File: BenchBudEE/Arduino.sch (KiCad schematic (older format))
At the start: 19 parts

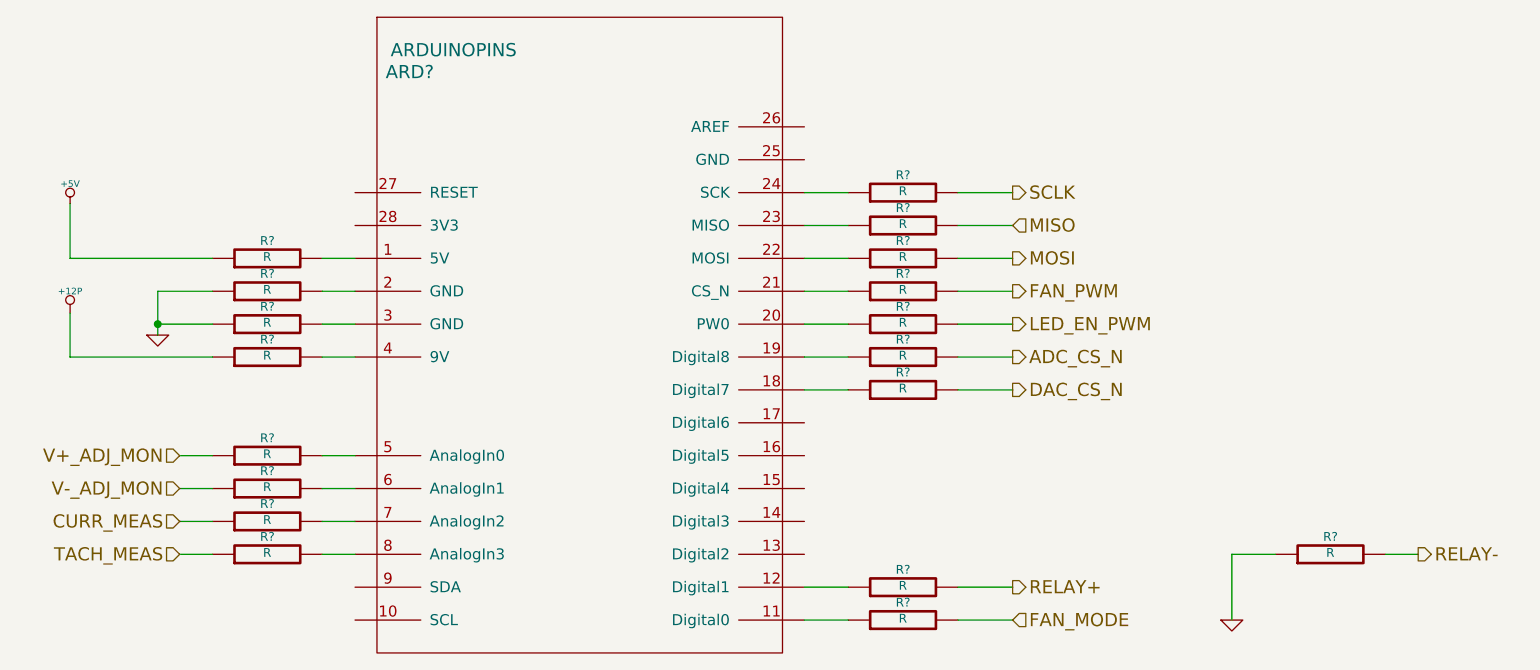
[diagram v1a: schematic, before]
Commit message: Associating and Placing the Relay Module
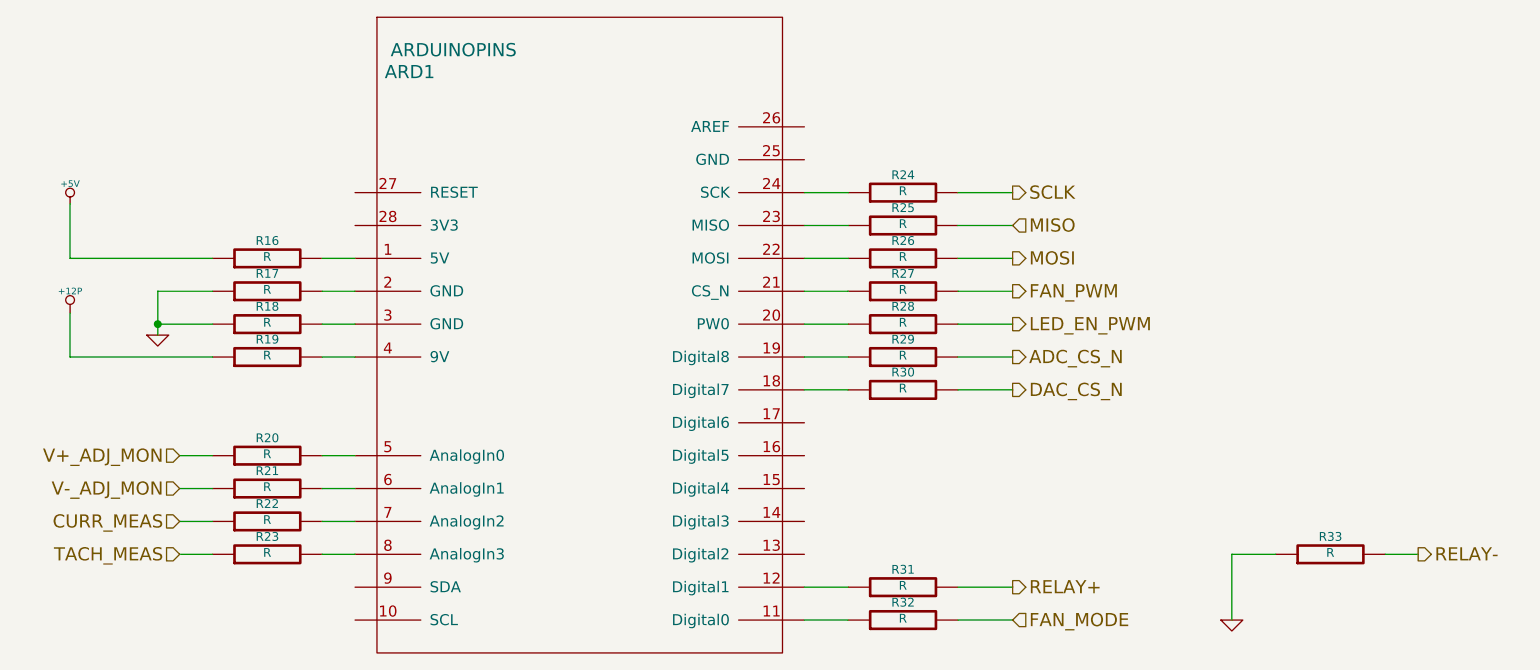
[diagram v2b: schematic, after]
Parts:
- gave numbers to parts that had none: 19
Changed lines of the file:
@@
 CURR_MEAS
 $Comp
-L R R?
+L R R27
 U 1 1 52F7E8CB
 P 6200 4350
-F 0 "R?" V 6280 4350 40  0000 C CNN
+F 0 "R27" V 6280 4350 40  0000 C CNN
 F 1 "R" V 6207 4351 40  0000 C CNN
 F 2 "~" V 6130 4350 30  0000 C CNN
@@
 	6450 4350 6700 4350
 $Comp
-L R R?
+L R R31
 U 1 1 52F7FF15
 P 6200 5700
-F 0 "R?" V 6280 5700 40  0000 C CNN
+F 0 "R31" V 6280 5700 40  0000 C CNN
 F 1 "R" V 6207 5701 40  0000 C CNN
 F 2 "~" V 6130 5700 30  0000 C CNN
@@
 	7700 5550 7700 5850
 $Comp
-L GND #PWR034
+L GND #PWR39
 U 1 1 52F7FF5C
 P 7700 5850
-F 0 "#PWR034" H 7700 5850 30  0001 C CNN
+F 0 "#PWR39" H 7700 5850 30  0001 C CNN
 F 1 "GND" H 7700 5780 30  0001 C CNN
 F 2 "" H 7700 5850 60  0000 C CNN
@@
 $EndComp
 $Comp
-L R R?
+L R R22
 U 1 1 52F7FF69
 P 3300 5400
-F 0 "R?" V 3380 5400 40  0000 C CNN
+F 0 "R22" V 3380 5400 40  0000 C CNN
 F 1 "R" V 3307 5401 40  0000 C CNN
 F 2 "~" V 3230 5400 30  0000 C CNN
@@
 $EndComp
 $Comp
-L R R?
+L R R23
 U 1 1 52F7FF6F
 P 3300 5550
-F 0 "R?" V 3380 5550 40  0000 C CNN
+F 0 "R23" V 3380 5550 40  0000 C CNN
 F 1 "R" V 3307 5551 40  0000 C CNN
 F 2 "~" V 3230 5550 30  0000 C CNN
@@
 V-_ADJ_MON
 $Comp
-L R R?
+L R R21
 U 1 1 52F82BA9
 P 3300 5250
-F 0 "R?" V 3380 5250 40  0000 C CNN
+F 0 "R21" V 3380 5250 40  0000 C CNN
 F 1 "R" V 3307 5251 40  0000 C CNN
 F 2 "~" V 3230 5250 30  0000 C CNN
@@
 $EndComp
 $Comp
-L R R?
+L R R20
 U 1 1 52F82BAF
 P 3300 5100
-F 0 "R?" V 3380 5100 40  0000 C CNN
+F 0 "R20" V 3380 5100 40  0000 C CNN
 F 1 "R" V 3307 5101 40  0000 C CNN
 F 2 "~" V 3230 5100 30  0000 C CNN
@@
 	3550 5100 3700 5100
 $Comp
-L R R?
+L R R30
 U 1 1 52F82BF7
 P 6200 4800
-F 0 "R?" V 6280 4800 40  0000 C CNN
+F 0 "R30" V 6280 4800 40  0000 C CNN
 F 1 "R" V 6207 4801 40  0000 C CNN
 F 2 "~" V 6130 4800 30  0000 C CNN
@@
 $EndComp
 $Comp
-L R R?
+L R R26
 U 1 1 52F82BFD
 P 6200 4200
-F 0 "R?" V 6280 4200 40  0000 C CNN
+F 0 "R26" V 6280 4200 40  0000 C CNN
 F 1 "R" V 6207 4201 40  0000 C CNN
 F 2 "~" V 6130 4200 30  0000 C CNN
@@
 $EndComp
 $Comp
-L R R?
+L R R25
 U 1 1 52F82C03
 P 6200 4050
-F 0 "R?" V 6280 4050 40  0000 C CNN
+F 0 "R25" V 6280 4050 40  0000 C CNN
 F 1 "R" V 6207 4051 40  0000 C CNN
 F 2 "~" V 6130 4050 30  0000 C CNN
@@
 $EndComp
 $Comp
-L R R?
+L R R24
 U 1 1 52F82C09
 P 6200 3900
-F 0 "R?" V 6280 3900 40  0000 C CNN
+F 0 "R24" V 6280 3900 40  0000 C CNN
 F 1 "R" V 6207 3901 40  0000 C CNN
 F 2 "~" V 6130 3900 30  0000 C CNN
@@
 	6700 3900 6450 3900
 $Comp
-L R R?
+L R R33
 U 1 1 52F82CA5
 P 8150 5550
-F 0 "R?" V 8230 5550 40  0000 C CNN
+F 0 "R33" V 8230 5550 40  0000 C CNN
 F 1 "R" V 8157 5551 40  0000 C CNN
 F 2 "~" V 8080 5550 30  0000 C CNN
@@
 LED_EN_PWM
 $Comp
-L R R?
+L R R28
 U 1 1 52F82CFD
 P 6200 4500
-F 0 "R?" V 6280 4500 40  0000 C CNN
+F 0 "R28" V 6280 4500 40  0000 C CNN
 F 1 "R" V 6207 4501 40  0000 C CNN
 F 2 "~" V 6130 4500 30  0000 C CNN
@@
 	6450 4500 6700 4500
 $Comp
-L R R?
+L R R29
 U 1 1 52F85651
 P 6200 4650
-F 0 "R?" V 6280 4650 40  0000 C CNN
+F 0 "R29" V 6280 4650 40  0000 C CNN
 F 1 "R" V 6207 4651 40  0000 C CNN
 F 2 "~" V 6130 4650 30  0000 C CNN
@@
 FAN_MODE
 $Comp
-L R R?
+L R R32
 U 1 1 52FACCB6
 P 6200 5850
-F 0 "R?" V 6280 5850 40  0000 C CNN
+F 0 "R32" V 6280 5850 40  0000 C CNN
 F 1 "R" V 6207 5851 40  0000 C CNN
 F 2 "~" V 6130 5850 30  0000 C CNN
@@
 	6450 5850 6700 5850
 $Comp
-L R R?
+L R R19
 U 1 1 52FACD1D
 P 3300 4650
-F 0 "R?" V 3380 4650 40  0000 C CNN
+F 0 "R19" V 3380 4650 40  0000 C CNN
 F 1 "R" V 3307 4651 40  0000 C CNN
 F 2 "~" V 3230 4650 30  0000 C CNN
@@
 	2400 4650 2400 4450
 $Comp
-L +12P #PWR035
+L +12P #PWR37
 U 1 1 52FACD63
 P 2400 4450
-F 0 "#PWR035" H 2400 4420 30  0001 C CNN
+F 0 "#PWR37" H 2400 4420 30  0001 C CNN
 F 1 "+12P" H 2400 4550 30  0000 C CNN
 F 2 "" H 2400 4450 60  0000 C CNN
@@
 $EndComp
 $Comp
-L ARDUINOPINS ARD?
+L ARDUINOPINS ARD1
 U 1 1 52FF78C8
 P 4750 4650
-F 0 "ARD?" H 3950 5950 60  0000 C CNN
+F 0 "ARD1" H 3950 5950 60  0000 C CNN
 F 1 "ARDUINOPINS" H 4150 6050 60  0000 C CNN
 F 2 "~" H 4450 3700 60  0000 C CNN
@@
 	2400 4200 2400 3950
 $Comp
-L +5V #PWR036
+L +5V #PWR36
 U 1 1 5300B8CD
 P 2400 3950
-F 0 "#PWR036" H 2400 4040 20  0001 C CNN
+F 0 "#PWR36" H 2400 4040 20  0001 C CNN
 F 1 "+5V" H 2400 4040 30  0000 C CNN
 F 2 "" H 2400 3950 60  0000 C CNN
@@
 $EndComp
 $Comp
-L R R?
+L R R16
 U 1 1 5300B8E0
 P 3300 4200
-F 0 "R?" V 3380 4200 40  0000 C CNN
+F 0 "R16" V 3380 4200 40  0000 C CNN
 F 1 "R" V 3307 4201 40  0000 C CNN
 F 2 "~" V 3230 4200 30  0000 C CNN
@@
 $EndComp
 $Comp
-L R R?
+L R R17
 U 1 1 5300B8E6
 P 3300 4350
-F 0 "R?" V 3380 4350 40  0000 C CNN
+F 0 "R17" V 3380 4350 40  0000 C CNN
 F 1 "R" V 3307 4351 40  0000 C CNN
 F 2 "~" V 3230 4350 30  0000 C CNN
@@
 $EndComp
 $Comp
-L R R?
+L R R18
 U 1 1 5300B8EC
 P 3300 4500
-F 0 "R?" V 3380 4500 40  0000 C CNN
+F 0 "R18" V 3380 4500 40  0000 C CNN
 F 1 "R" V 3307 4501 40  0000 C CNN
 F 2 "~" V 3230 4500 30  0000 C CNN
@@
 Connection ~ 2800 4500
 $Comp
-L GND #PWR037
+L GND #PWR38
 U 1 1 5300B9FD
 P 2800 4550
-F 0 "#PWR037" H 2800 4550 30  0001 C CNN
+F 0 "#PWR38" H 2800 4550 30  0001 C CNN
 F 1 "GND" H 2800 4480 30  0001 C CNN
 F 2 "" H 2800 4550 60  0000 C CNN

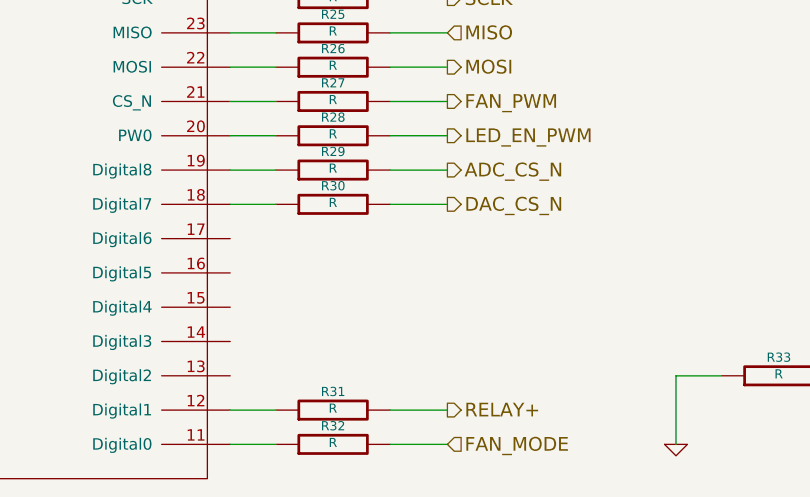
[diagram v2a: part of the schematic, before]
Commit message: Associating and Placingthe Thermocouple Module
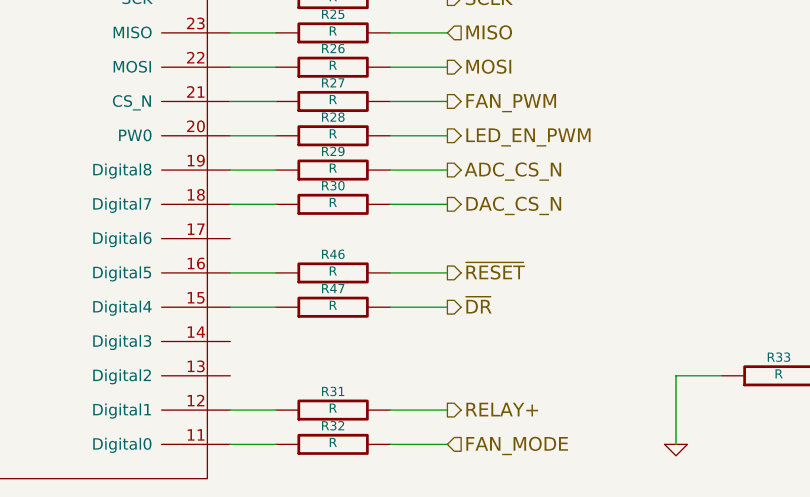
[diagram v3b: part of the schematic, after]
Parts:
- added R46, R47: R, ~, symbol R
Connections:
- net at ARD1.15 (Digital4): now also R47.1
- net at ARD1.16 (Digital5): now also R46.1
- new net ~DR: R47.2
- new net ~RESET: R46.2
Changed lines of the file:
@@
 Sheet 7 9
 Title ""
-Date "17 feb 2014"
+Date "19 feb 2014"
 Rev ""
 Comp ""
@@
 	7700 5550 7700 5850
 $Comp
-L GND #PWR39
+L GND #PWR042
 U 1 1 52F7FF5C
 P 7700 5850
-F 0 "#PWR39" H 7700 5850 30  0001 C CNN
+F 0 "#PWR042" H 7700 5850 30  0001 C CNN
 F 1 "GND" H 7700 5780 30  0001 C CNN
 F 2 "" H 7700 5850 60  0000 C CNN
@@
 	2400 4650 2400 4450
 $Comp
-L +12P #PWR37
+L +12P #PWR043
 U 1 1 52FACD63
 P 2400 4450
-F 0 "#PWR37" H 2400 4420 30  0001 C CNN
+F 0 "#PWR043" H 2400 4420 30  0001 C CNN
 F 1 "+12P" H 2400 4550 30  0000 C CNN
 F 2 "" H 2400 4450 60  0000 C CNN
@@
 	2400 4200 2400 3950
 $Comp
-L +5V #PWR36
+L +5V #PWR044
 U 1 1 5300B8CD
 P 2400 3950
-F 0 "#PWR36" H 2400 4040 20  0001 C CNN
+F 0 "#PWR044" H 2400 4040 20  0001 C CNN
 F 1 "+5V" H 2400 4040 30  0000 C CNN
 F 2 "" H 2400 3950 60  0000 C CNN
@@
 Connection ~ 2800 4500
 $Comp
-L GND #PWR38
+L GND #PWR045
 U 1 1 5300B9FD
 P 2800 4550
-F 0 "#PWR38" H 2800 4550 30  0001 C CNN
+F 0 "#PWR045" H 2800 4550 30  0001 C CNN
 F 1 "GND" H 2800 4480 30  0001 C CNN
 F 2 "" H 2800 4550 60  0000 C CNN
@@
 	1    0    0    -1
 $EndComp
+Text HLabel 6700 5250 2    60   Output ~ 0
+~DR
+$Comp
+L R R47
+U 1 1 53041CC0
+P 6200 5250
+F 0 "R47" V 6280 5250 40  0000 C CNN
+F 1 "R" V 6207 5251 40  0000 C CNN
+F 2 "~" V 6130 5250 30  0000 C CNN
+F 3 "~" H 6200 5250 30  0000 C CNN
+	1    6200 5250
+	0    -1   -1   0
+$EndComp
+Wire Wire Line
+	5750 5250 5950 5250
+Wire Wire Line
+	6450 5250 6700 5250
+$Comp
+L R R46
+U 1 1 53041CC8
+P 6200 5100
+F 0 "R46" V 6280 5100 40  0000 C CNN
+F 1 "R" V 6207 5101 40  0000 C CNN
+F 2 "~" V 6130 5100 30  0000 C CNN
+F 3 "~" H 6200 5100 30  0000 C CNN
+	1    6200 5100
+	0    -1   -1   0
+$EndComp
+Wire Wire Line
+	5750 5100 5950 5100
+Wire Wire Line
+	6450 5100 6700 5100
+Text HLabel 6700 5100 2    60   Output ~ 0
+~RESET
 $EndSCHEMATC

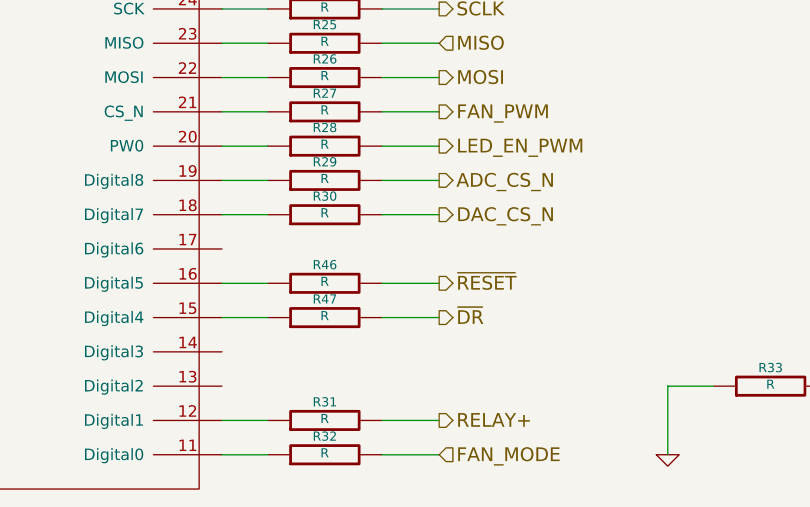
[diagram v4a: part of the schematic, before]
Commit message: Associating and Placing Fan Module
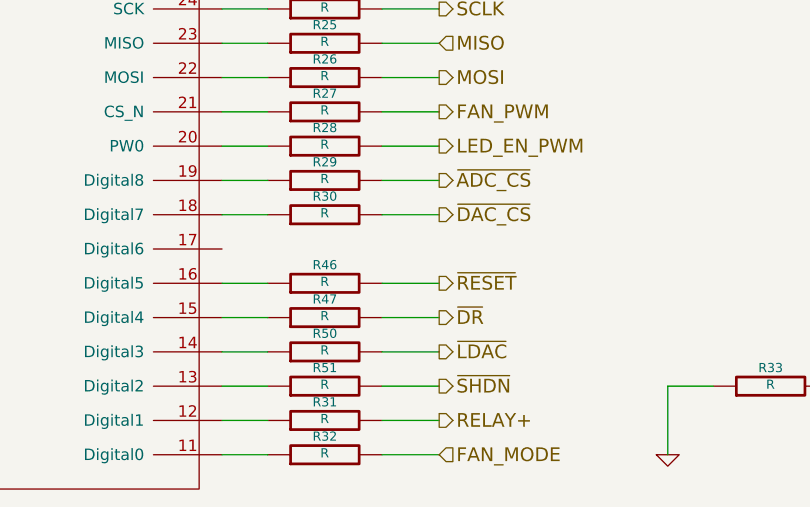
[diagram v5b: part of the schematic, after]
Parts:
- added R50, R51: R, ~, symbol R
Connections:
- net at ARD1.13 (Digital2): now also R51.1
- net at ARD1.14 (Digital3): now also R50.1
- net ADC_CS_N renamed ~ADC_CS
- net DAC_CS_N renamed ~DAC_CS
- new net ~LDAC: R50.2
- new net ~SHDN: R51.2
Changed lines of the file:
@@
 SCLK
 Text HLabel 6700 4800 2    60   Output ~ 0
-DAC_CS_N
+~DAC_CS
 Text HLabel 6700 4350 2    60   Output ~ 0
 FAN_PWM
@@
 	7700 5550 7700 5850
 $Comp
-L GND #PWR042
+L GND #PWR47
 U 1 1 52F7FF5C
 P 7700 5850
-F 0 "#PWR042" H 7700 5850 30  0001 C CNN
+F 0 "#PWR47" H 7700 5850 30  0001 C CNN
 F 1 "GND" H 7700 5780 30  0001 C CNN
 F 2 "" H 7700 5850 60  0000 C CNN
@@
 $EndComp
 Text HLabel 6700 4650 2    60   Output ~ 0
-ADC_CS_N
+~ADC_CS
 Wire Wire Line
 	5750 4650 5950 4650
@@
 	2400 4650 2400 4450
 $Comp
-L +12P #PWR043
+L +12P #PWR45
 U 1 1 52FACD63
 P 2400 4450
-F 0 "#PWR043" H 2400 4420 30  0001 C CNN
+F 0 "#PWR45" H 2400 4420 30  0001 C CNN
 F 1 "+12P" H 2400 4550 30  0000 C CNN
 F 2 "" H 2400 4450 60  0000 C CNN
@@
 	2400 4200 2400 3950
 $Comp
-L +5V #PWR044
+L +5V #PWR44
 U 1 1 5300B8CD
 P 2400 3950
-F 0 "#PWR044" H 2400 4040 20  0001 C CNN
+F 0 "#PWR44" H 2400 4040 20  0001 C CNN
 F 1 "+5V" H 2400 4040 30  0000 C CNN
 F 2 "" H 2400 3950 60  0000 C CNN
@@
 Connection ~ 2800 4500
 $Comp
-L GND #PWR045
+L GND #PWR46
 U 1 1 5300B9FD
 P 2800 4550
-F 0 "#PWR045" H 2800 4550 30  0001 C CNN
+F 0 "#PWR46" H 2800 4550 30  0001 C CNN
 F 1 "GND" H 2800 4480 30  0001 C CNN
 F 2 "" H 2800 4550 60  0000 C CNN
@@
 Text HLabel 6700 5100 2    60   Output ~ 0
 ~RESET
+$Comp
+L R R50
+U 1 1 5308D04B
+P 6200 5400
+F 0 "R50" V 6280 5400 40  0000 C CNN
+F 1 "R" V 6207 5401 40  0000 C CNN
+F 2 "~" V 6130 5400 30  0000 C CNN
+F 3 "~" H 6200 5400 30  0000 C CNN
+	1    6200 5400
+	0    -1   -1   0
+$EndComp
+$Comp
+L R R51
+U 1 1 5308D051
+P 6200 5550
+F 0 "R51" V 6280 5550 40  0000 C CNN
+F 1 "R" V 6207 5551 40  0000 C CNN
+F 2 "~" V 6130 5550 30  0000 C CNN
+F 3 "~" H 6200 5550 30  0000 C CNN
+	1    6200 5550
+	0    -1   -1   0
+$EndComp
+Text HLabel 6700 5550 2    60   Output ~ 0
+~SHDN
+Wire Wire Line
+	6450 5550 6700 5550
+Text HLabel 6700 5400 2    60   Output ~ 0
+~LDAC
+Wire Wire Line
+	6450 5400 6700 5400
+Wire Wire Line
+	5950 5400 5750 5400
+Wire Wire Line
+	5750 5550 5950 5550
 $EndSCHEMATC
